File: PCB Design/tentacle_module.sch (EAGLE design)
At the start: 40 parts, among them IC1 5V, X3 RJ45-8X, X4 RJ45-8X

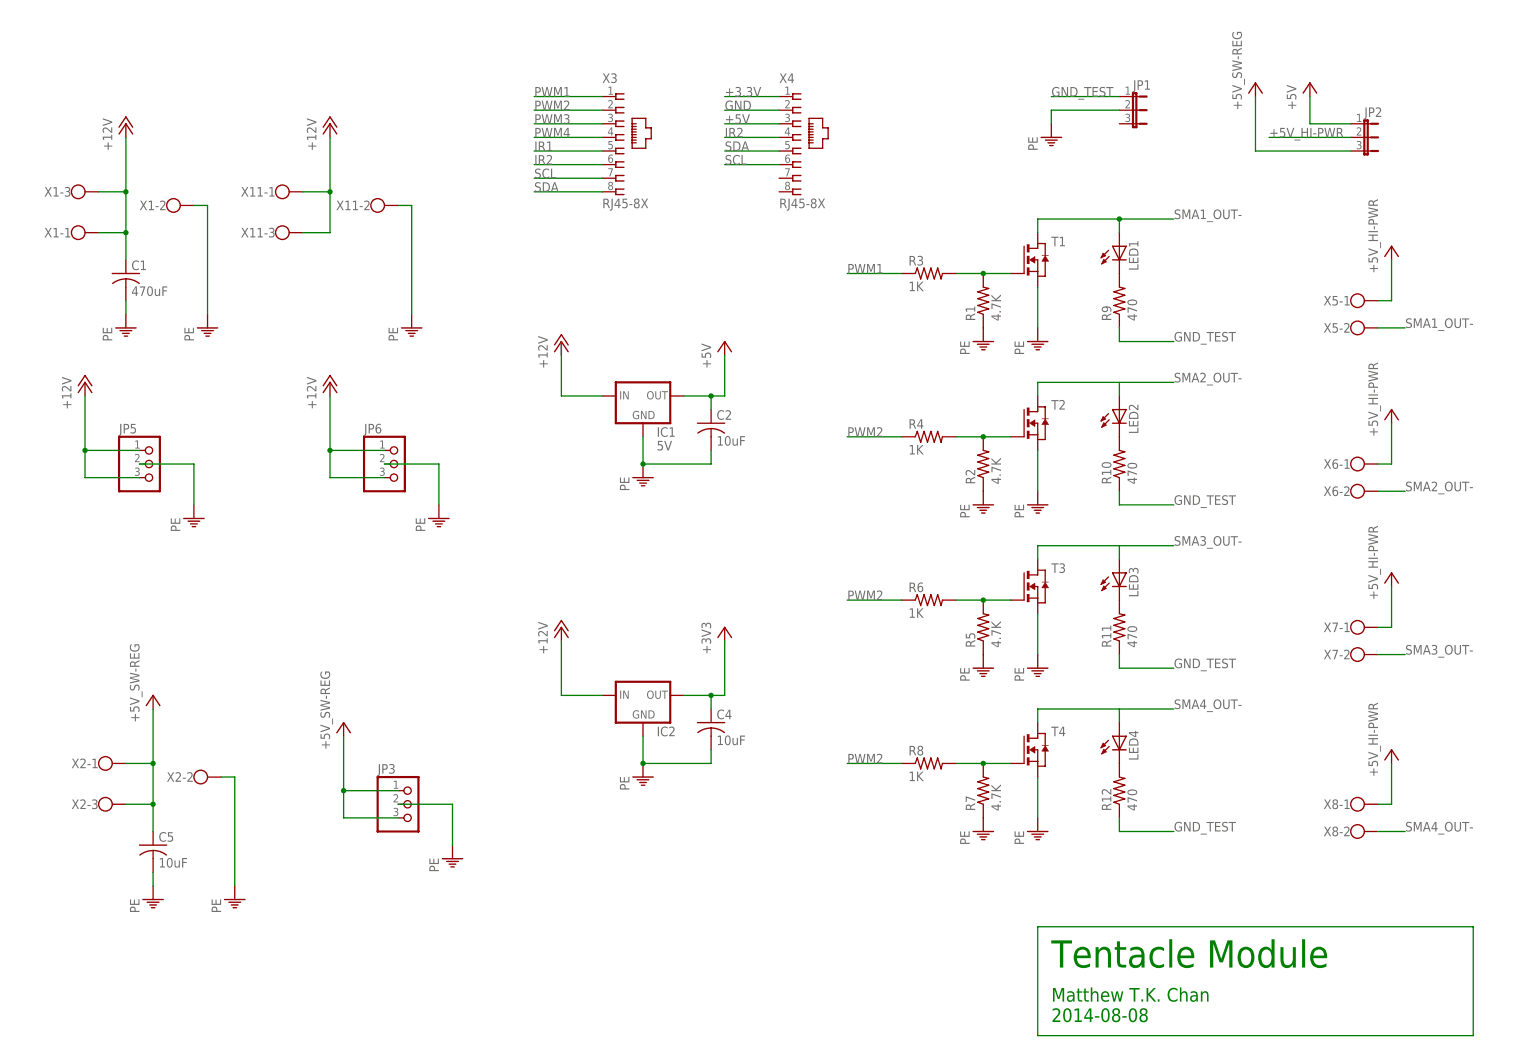
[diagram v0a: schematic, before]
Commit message: fixed the indicator LED error.
The negative pin of the LED was connected to the ground and the positive
pin was connected to the drain. That wouldn't have worked.
Also rotated the longer labels to make them fit nicer.
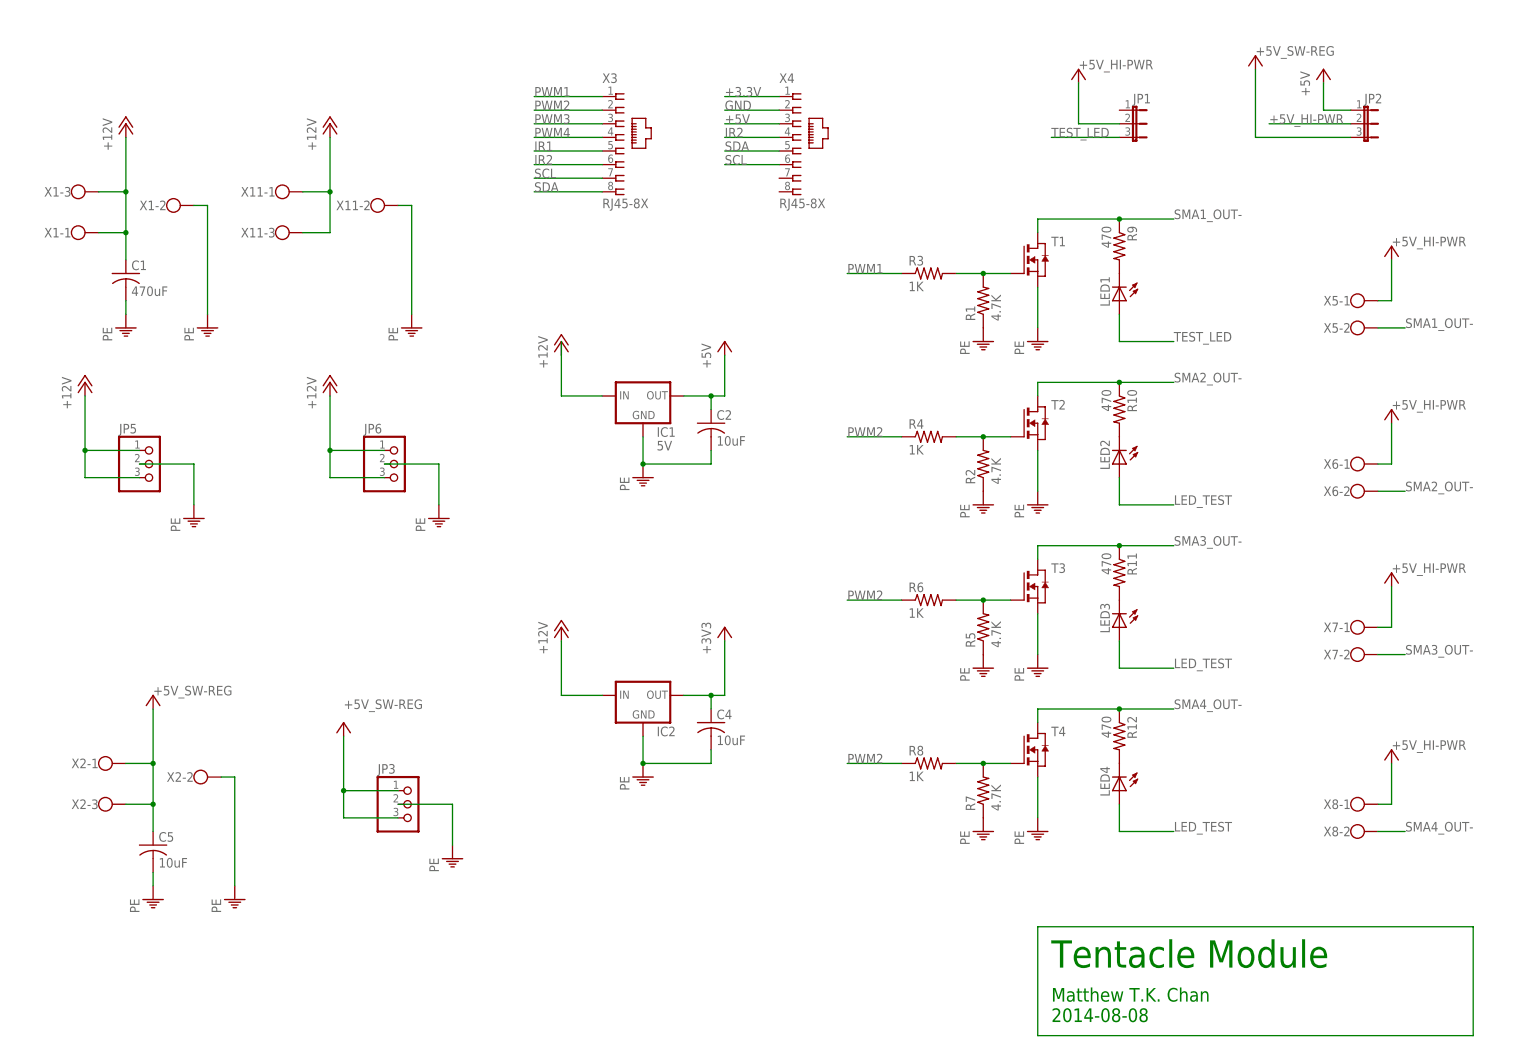
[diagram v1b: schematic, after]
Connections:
- removed net GND_TEST: JP1.1, R10.1, R11.1, R12.1, R9.1
- removed net SMA1_OUT-1: LED2.A
- removed net SMA1_OUT-2: LED3.A
- removed net SMA1_OUT-3: LED4.A
- new net LED_TEST: LED2.A, LED3.A, LED4.A
- new net TEST_LED: JP1.3, LED1.A
- net +5V: now also JP1.2
- net GND: no longer JP1.2
- net SMA1_OUT-: now also R9.1; no longer LED1.A
- net SMA2_OUT-: now also R10.1
- net SMA3_OUT-: now also R11.1
- net SMA4_OUT-: now also R12.1
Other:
- moved on the sheet: JP1, JP2, LED1, LED2, LED3, LED4, R10, R11, R12, R9

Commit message: Tentacle board improvement
Added Schottky diodes for reverse voltage protection
Added headers fro the RJ45 jack for more flexibility in terms of
connectors
Added modified the appearance of the schematic and added some more
comments.
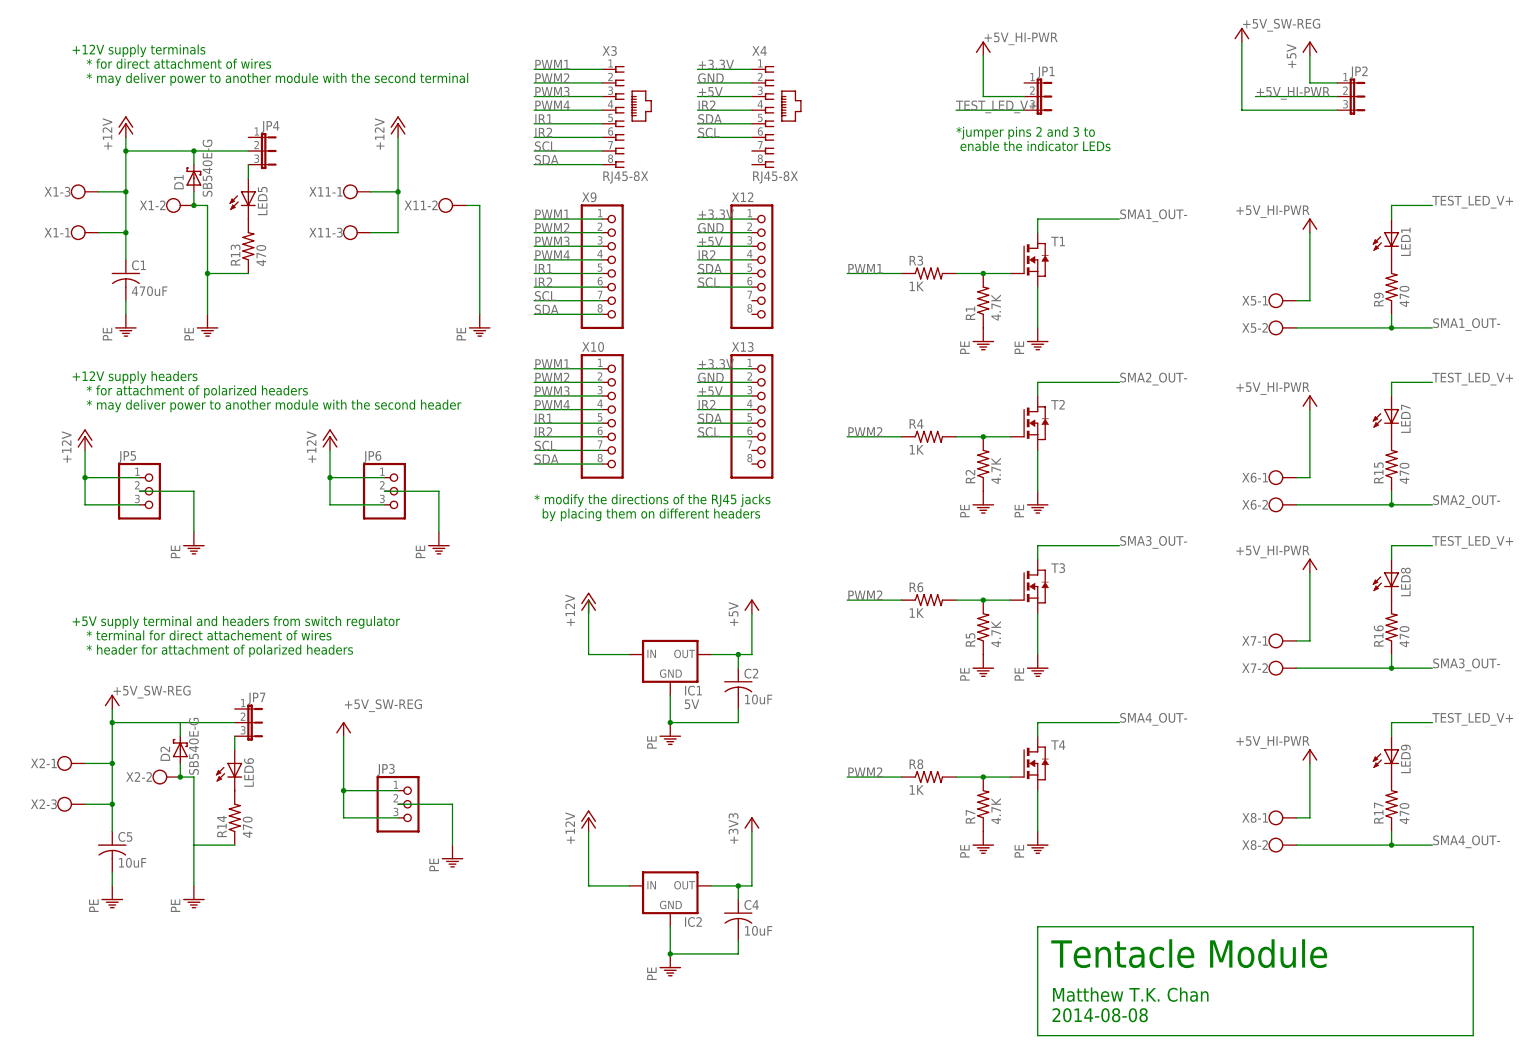
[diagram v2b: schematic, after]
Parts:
- removed LED2, LED3, LED4: (no value), led:LEDSML1206
- removed R10, R11, R12: 470, rcl:R-US_R1206
- added D1, D2: SB540E-G, CBLA_Test_bed_Library:SB540E-G
- added JP4, JP7: (no value), jumper:JP2W
- added LED5, LED6, LED7, LED8, LED9: (no value), led:LEDSML1206
- added R13, R14, R15, R16, R17: 470, rcl:R-US_R1206
- added X10, X12, X13, X9: (no value), pinhead:PINHD-1X8/90
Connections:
- removed net LED_TEST: LED2.A, LED3.A, LED4.A
- removed net N$6: LED2.C, R10.2
- removed net N$7: LED3.C, R11.2
- removed net N$8: LED4.C, R12.2
- removed net TEST_LED: JP1.3, LED1.A
- new net +12V1: JP7.2
- new net GND1: R14.1
- new net N$10: LED5.C, R13.2
- new net N$11: JP4.3, LED5.A
- new net N$12: LED6.C, R14.2
- new net N$13: JP7.3, LED6.A
- new net N$14: LED7.C, R15.2
- new net N$15: LED8.C, R16.2
- new net N$16: LED9.C, R17.2
- new net TEST_LED_V+: JP1.3, LED1.A, LED7.A, LED8.A, LED9.A
- net +12V: now also D1.C, JP4.2
- net +3.3V: now also X12.1, X13.1
- net +5V: now also X12.3, X13.3
- net +5V_SW-REG: now also D2.C
- net GND: now also D1.A, D2.A, R13.1, X12.2, X13.2
- net IR1: now also X10.5, X9.5
- net IR2: now also X10.6, X12.4, X13.4, X9.6
- net PWM1: now also X10.1, X9.1
- net PWM2: now also X10.2, X9.2
- net PWM3: now also X10.3, X9.3
- net PWM4: now also X10.4, X9.4
- net SCL: now also X10.7, X12.6, X13.6, X9.7
- net SDA: now also X10.8, X12.5, X13.5, X9.8
- net SMA2_OUT-: now also R15.1; no longer R10.1
- net SMA3_OUT-: now also R16.1; no longer R11.1
- net SMA4_OUT-: now also R17.1; no longer R12.1
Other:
- note added: "* modify the directions of the RJ45 jacks by placing them on different headers"
- note added: "*jumper pins 2 and 3 to enable the indicator LEDs"
- note added: "+12V supply headers * for attachment of polarized headers * may deliver power to another module with the second header"
- note added: "+12V supply terminals * for direct attachment of wires * may deliver power to another module with the second terminal"
- note added: "+5V supply terminal and headers from switch regulator * terminal for direct attachement of wires * header for attachment of polarized headers"
- moved on the sheet: C2, C4, C5, IC1, IC2, JP1, JP2, JP5, JP6, LED1, R7, R8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

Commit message: Positioned components on Tentacle PCB
Fixed some mistakes on the schematics
Remove one pair of the headers for the RJ45 port
Placed  components on the PCB.
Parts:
- removed X10, X13: (no value), pinhead:PINHD-1X8/90
- removed X11: (no value), con-wago-500:W237-103
- C2: device rcl:C-USC1210 -> rcl:C-USC1206
- IC1, IC2: device CBLA_Test_bed_Library:78XXS -> CBLA_Test_bed_Library:78XXSHORIZONTAL
- JP1, JP2, JP4, JP7: device jumper:JP2W -> jumper:JP2E
- T1, T2, T3, T4: value (none) -> NTD5867NL
- X1: device con-wago-500:W237-103 -> con-wago-508:W237-04P
- X2: device con-wago-500:W237-103 -> con-wago-508:W237-03P
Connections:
- net +12V: no longer X1-3.KL, X11-1.KL, X11-3.KL
- net +3.3V: no longer X13.1
- net +5V: no longer X13.3
- net GND: now also X1-3.KL; no longer X11-2.KL, X13.2
- net IR1: no longer X10.5
- net IR2: no longer X10.6, X13.4
- net PWM1: no longer X10.1
- net PWM2: no longer R6.1, R8.1, X10.2
- net PWM3: now also R6.1; no longer X10.3
- net PWM4: now also R8.1; no longer X10.4
- net SCL: no longer X10.7, X13.6
- net SDA: no longer X10.8, X13.5

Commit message: Changed capacitor footprint from 1210 to 1206
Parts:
- C1, C5: device rcl:C-USC1210 -> rcl:C-USC1206
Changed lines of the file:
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@@
 <part name="C4" library="rcl" deviceset="C-US" device="C1206" value="10uF"/>
 <part name="C2" library="rcl" deviceset="C-US" device="C1206" value="10uF"/>
-<part name="C5" library="rcl" deviceset="C-US" device="C1210" value="10uF"/>
+<part name="C5" library="rcl" deviceset="C-US" device="C1206" value="10uF"/>
 <part name="P+1" library="supply1" deviceset="+12V" device=""/>
 <part name="P+2" library="supply1" deviceset="+12V" device=""/>
@@
 <part name="PE16" library="supply1" deviceset="PE" device=""/>
 <part name="P+12" library="supply1" deviceset="+5V" device="" value="+5V_SW-REG"/>
-<part name="C1" library="rcl" deviceset="C-US" device="C1210" value="470uF"/>
+<part name="C1" library="rcl" deviceset="C-US" device="C1206" value="470uF"/>
 <part name="PE18" library="supply1" deviceset="PE" device=""/>
 <part name="PE19" library="supply1" deviceset="PE" device=""/>
